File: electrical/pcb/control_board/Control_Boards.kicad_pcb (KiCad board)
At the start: 2 copper layers, 220 x 367.6 mm, 141 parts, among them J1 XT30-M, J10 Molex_172675-0613, J11 Molex_172675-0613, J13 Molex_172675-0613, J14 Molex_172675-0613, J16 277-11404-ND, J17 277-11404-ND, J18 277-11404-ND, J19 TSW-104-07-F-T, J2 ED2580-ND, J20 PEC08SAAN, J21 PPTC102LFBN-RC, J22 S9175-ND_rpi_breakout, J23 S9175-ND_rpi_breakout, J24 6posheader, J25 SSW-104-01-F-T, J26 WM6548-ND, J27 PPTC021LFBN-RC, J28 PPTC021LFBN-RC, J29 PPTC021LFBN-RC, J3 XT30-F, J30 PEC08SAAN, J4 XT30-F, J5 XT30-M, J6 ED2580-ND, J8 Molex_172675-0613, J9 Molex_172675-0613, M1 Mounting_Holes, Q1 2N3906, Q2 2N3906, Q3 2N3906, Q4 2N3906, Q5 2N3906, Q6 2N3906, SW1 CT206124-ND, T1 test_point, T10 test_point, T11 test_point, T12 test_point, T13 test_point, T14 test_point, T15 test_point, T2 test_point, T3 test_point, T4 test_point, T5 test_point, T6 test_point, T7 test_point, T8 test_point, T9 test_point, U1 INA260, U2 PCA9685, U3 D24V22Fx, U4 D24V150Fx, U5 DC7G3HWA, U6 DC7G3HWA, U7 MIC2937A-3.3WT, y1 rover_silkscreen

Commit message: updates
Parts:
- moved J17 89.4 mm to (214.3, 85.7), turned to 90 degrees
- moved RC2 63.3 mm to (145.8, 59.3), turned to 270 degrees
- moved C3 31.4 mm to (97.1, 90.6), turned to 90 degrees
- moved R21 22.9 mm to (66.0, 34.4), turned to 90 degrees
- moved C13 18.0 mm to (192.2, 70.9), turned to 180 degrees
- moved C15 18.0 mm to (192.2, 74.1), turned to 180 degrees
- moved C17 17.9 mm to (192.2, 77.2), turned to 180 degrees
- moved C20 17.9 mm to (192.2, 80.4), turned to 180 degrees
- moved C2 17.8 mm to (156.2, 70.8), turned to 0 degrees
- moved C4 11.2 mm to (156.2, 74.1), turned to 0 degrees
- moved C1 5.28 mm to (118.7, 49.0)
- moved RC1 5.16 mm to (202.6, 59.3)
- moved J16 4.97 mm to (132.1, 78.3)
- moved R5 4.78 mm to (122.0, 56.6)
- moved C9 4.68 mm to (156.2, 77.5), turned to 0 degrees
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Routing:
- net /Motor Board/E_STOP3: track 0.00 -> 417.0 mm, vias 0 -> 6
- net /Motor Board/E_STOP2: track 0.00 -> 403.5 mm, vias 0 -> 7
- net /Motor Board/E_STOP: track 0.00 -> 398.3 mm, vias 0 -> 6
- net /Motor Board/RXD: track 0.00 -> 347.5 mm, vias 0 -> 4
- net /Motor Board/TXD: track 0.00 -> 342.0 mm, vias 0 -> 4
- net /Motor Board/BATTPOS: track 0.00 -> 300.1 mm, vias 0 -> 7
- net +3.3V_motor: track 212.6 -> 402.2 mm, vias 6 -> 11
- net /Motor Board/RC2M1A: track 172.1 -> 296.4 mm, vias 4 -> 6
- net /Motor Board/alert: track 0.00 -> 118.2 mm, vias 0 -> 4
- net /Motor Board/RC2M1B: track 171.6 -> 289.5 mm, vias 4 -> 6
- net +BATT: track 0.00 -> 104.7 mm, vias 0 -> 3
- net /Motor Board/RC2M2A: track 155.9 -> 255.5 mm, vias 4 -> 6
- net /Motor Board/SDA_rpi: track 0.00 -> 97.7 mm, vias 0 -> 5
- net /Motor Board/SCL_rpi: track 0.00 -> 95.1 mm, vias 0 -> 5
- net /Motor Board/RC2M2B: track 163.6 -> 255.8 mm, vias 4 -> 6
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
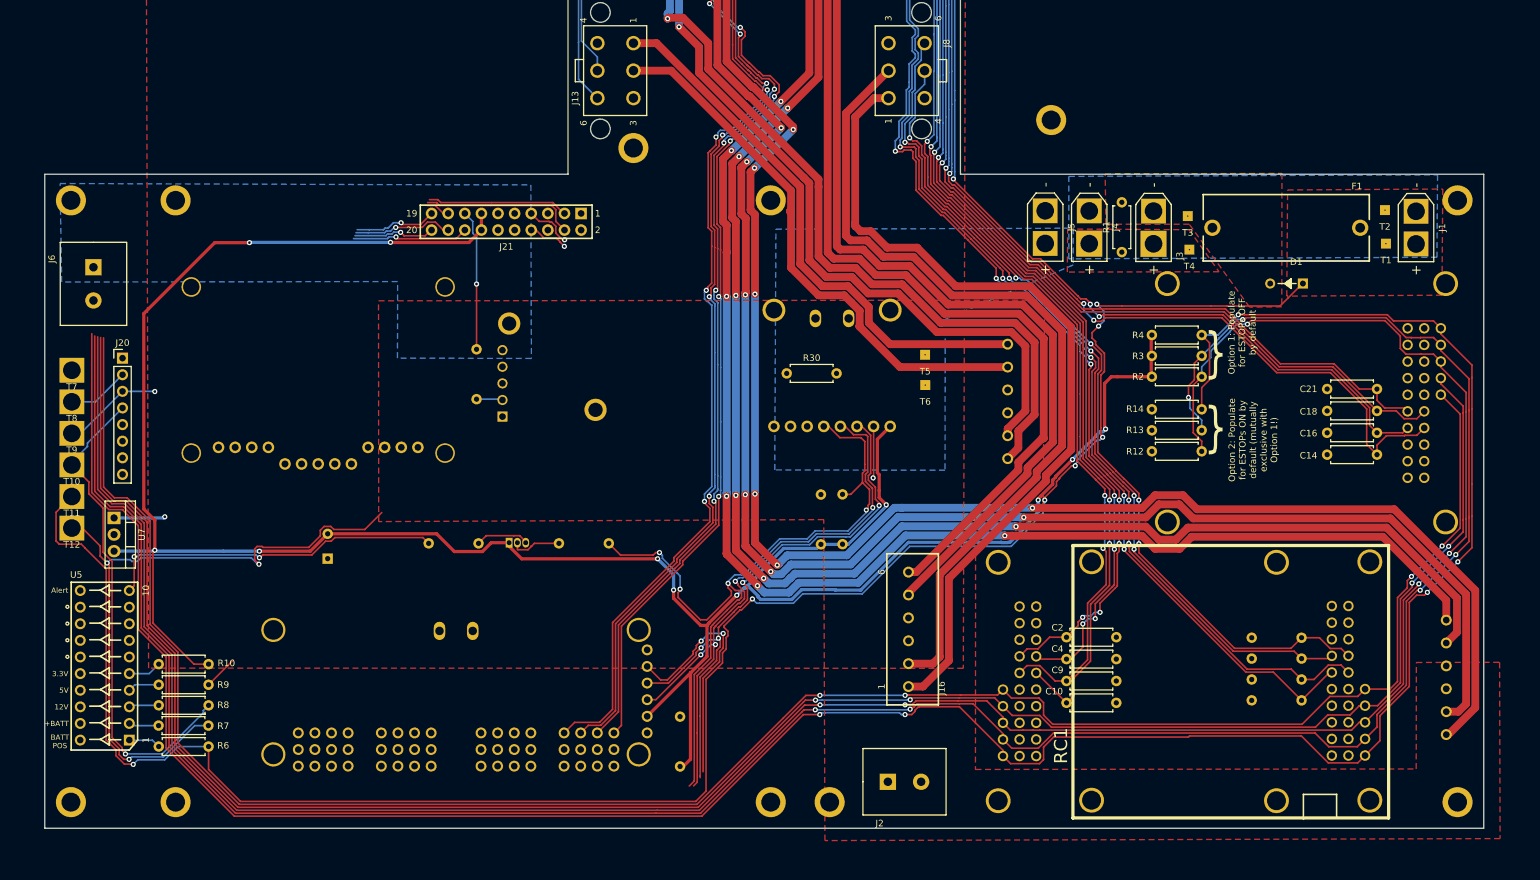
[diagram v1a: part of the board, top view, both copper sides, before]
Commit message: finished routing of motor board
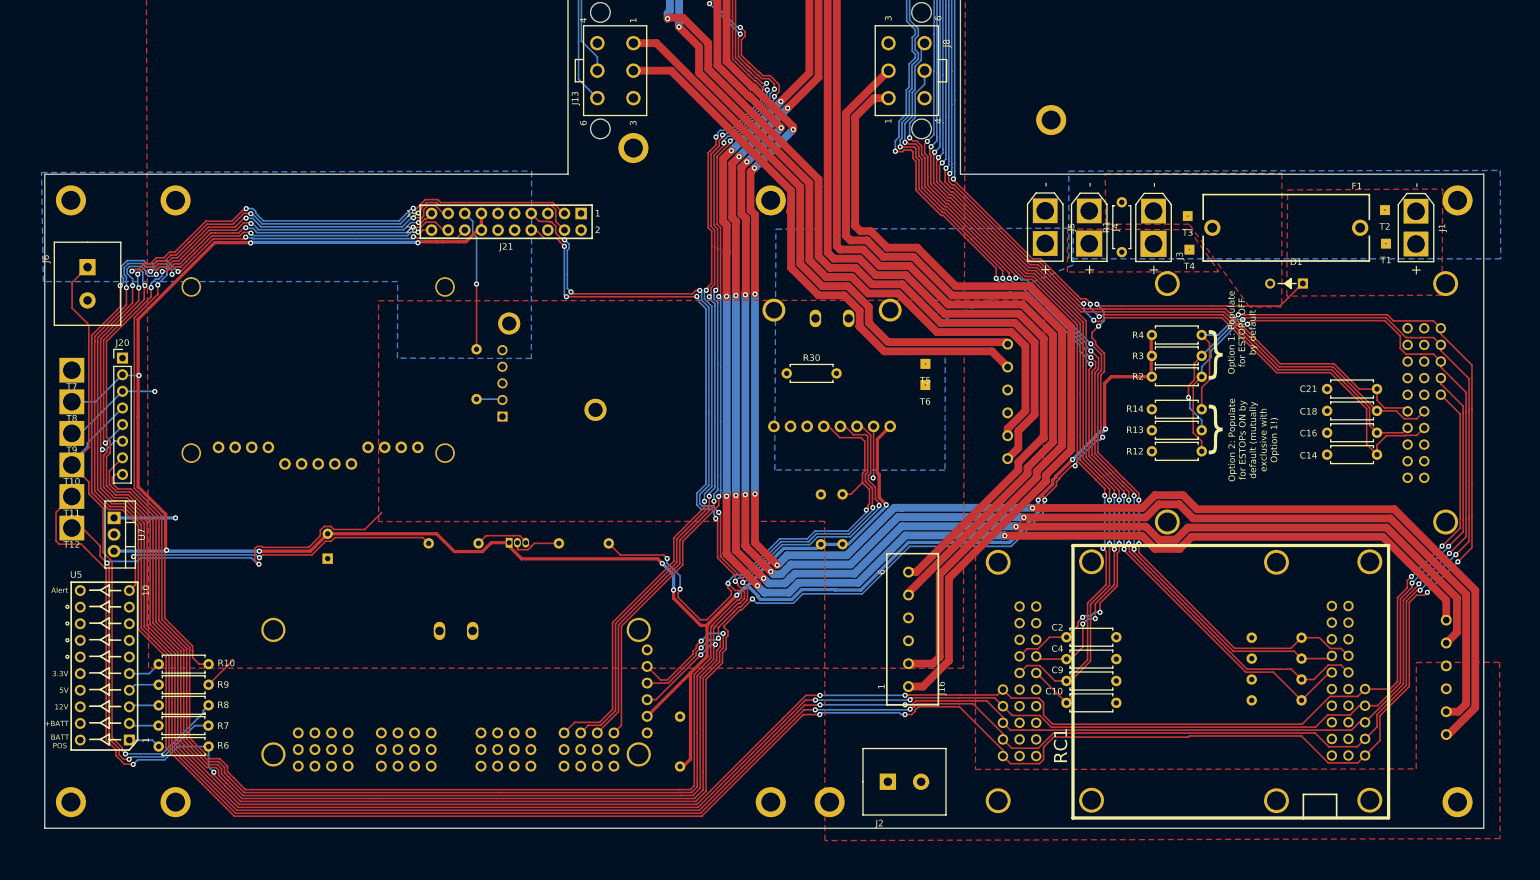
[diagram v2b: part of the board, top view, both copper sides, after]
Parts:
- moved T5 1.39 mm to (134.6, 29.0)
- moved J6 0.90 mm to (6.54, 14.2)
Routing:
- net /Motor Board/SCL_rpi: track 95.1 -> 308.1 mm, vias 5 -> 8
- net /Motor Board/alert: track 118.2 -> 327.3 mm, vias 4 -> 8
- net /Motor Board/SDA_rpi: track 97.7 -> 303.4 mm, vias 5 -> 8
- net /Motor Board/OEservos: track 53.6 -> 255.8 mm, vias 3 -> 6
- net /Motor Board/TXD: track 342.0 -> 413.3 mm, vias 4 -> 9
- net /Motor Board/RXD: track 347.5 -> 414.3 mm, vias 4 -> 9
- net /Motor Board/E_STOP: track 398.3 -> 451.4 mm, vias 6 -> 9
- net /Motor Board/E_STOP2: track 403.5 -> 456.0 mm, vias 7 -> 10
- net /Motor Board/E_STOP3: track 417.0 -> 468.5 mm, vias 6 -> 9
- net +12V_motor: track 75.5 -> 108.8 mm
- net +3.3V_motor: track 402.2 -> 404.7 mm, vias 11 -> 12
- net +5V_motor: track 36.1 -> 37.7 mm
- net /Motor Board/servo_pwm_ch3: track 187.6 -> 187.1 mm
- net /Motor Board/BATTPOS: track 300.1 -> 300.2 mm, vias 7 -> 8

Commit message: progress on brain board
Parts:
- moved R11 29.5 mm to (96.1, -190.0)
- moved J25 9.34 mm to (92.6, -171.4), turned to 90 degrees
- moved SW1 4.81 mm to (103.4, -215.5)
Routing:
- net GND_brain: track 0.00 -> 90.8 mm
- net /Brain Board/E_STOP: track 0.00 -> 61.6 mm
- net /Brain Board/E_STOP3: track 0.00 -> 59.4 mm
- net /Brain Board/E_STOP2: track 0.00 -> 54.0 mm
- net /Brain Board/SCL_rpi: track 0.00 -> 40.0 mm, vias 0 -> 1
- net /Brain Board/SDA_rpi: track 0.00 -> 36.2 mm, vias 0 -> 1
- net /Brain Board/OEservos: track 0.00 -> 34.7 mm
- net /Brain Board/12V_EN: track 0.00 -> 32.9 mm
- net /Brain Board/alert: track 0.00 -> 30.2 mm
- net +12V_brain: track 0.00 -> 28.0 mm, vias 0 -> 1
- net +5V_brain: track 0.00 -> 25.2 mm
- net /Brain Board/3.3V_rpi: track 0.00 -> 22.7 mm
- net /Brain Board/X_RPI_SPI_MISO: track 0.00 -> 11.3 mm
- net /Brain Board/X_RPI_SPI_CLK: track 0.00 -> 11.3 mm
- net /Brain Board/X_RPI_GPIO_GCLK: track 0.00 -> 11.3 mm
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- added copper zone on F.Cu, net +3.3V_brain
- added copper zone on B.Cu, net GND_brain

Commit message: progress on brain board
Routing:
- net +5V_brain: track 25.2 -> 155.4 mm, vias 0 -> 5
- net /Brain Board/RXD: track 11.3 -> 135.9 mm, vias 0 -> 5
- net /Brain Board/TXD: track 11.3 -> 133.1 mm, vias 0 -> 5
- net /Brain Board/SDA_rpi: track 36.2 -> 147.0 mm, vias 1 -> 3
- net /Brain Board/SCL_rpi: track 40.0 -> 145.8 mm, vias 1 -> 5
- net /Brain Board/OEservos: track 34.7 -> 134.7 mm, vias 0 -> 1
- net +12V_brain: track 28.0 -> 126.7 mm, vias 1 -> 3
- net /Brain Board/alert: track 30.2 -> 91.4 mm
- net /Brain Board/12V_EN: track 32.9 -> 92.5 mm
- net /Brain Board/ESTOP_in_2: track 0.00 -> 41.3 mm
- net /Brain Board/E_STOP3: track 59.4 -> 97.6 mm
- net /Brain Board/ESTOP_in_3: track 0.00 -> 38.2 mm, vias 0 -> 1
- net /Brain Board/E_STOP2: track 54.0 -> 88.0 mm
- net /Brain Board/E_STOP: track 61.6 -> 91.3 mm

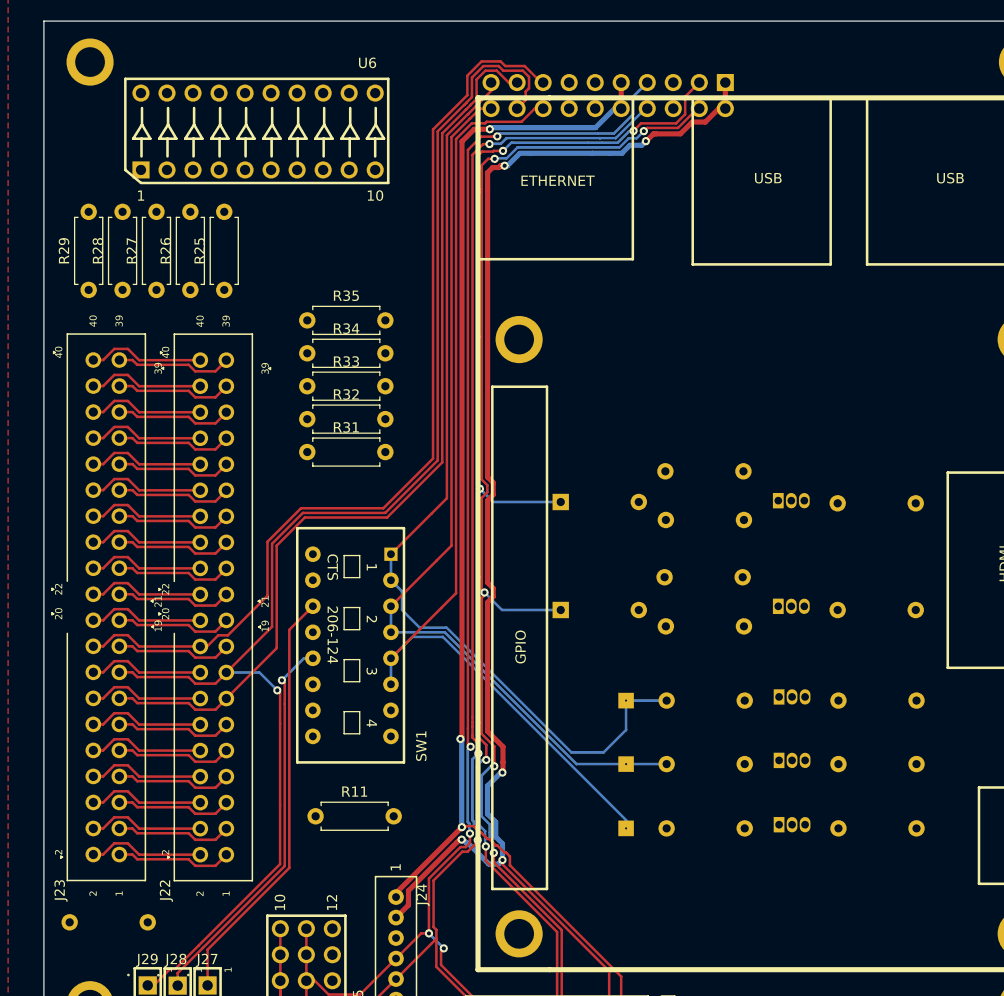
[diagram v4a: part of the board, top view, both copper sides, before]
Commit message: Finished routing brain board
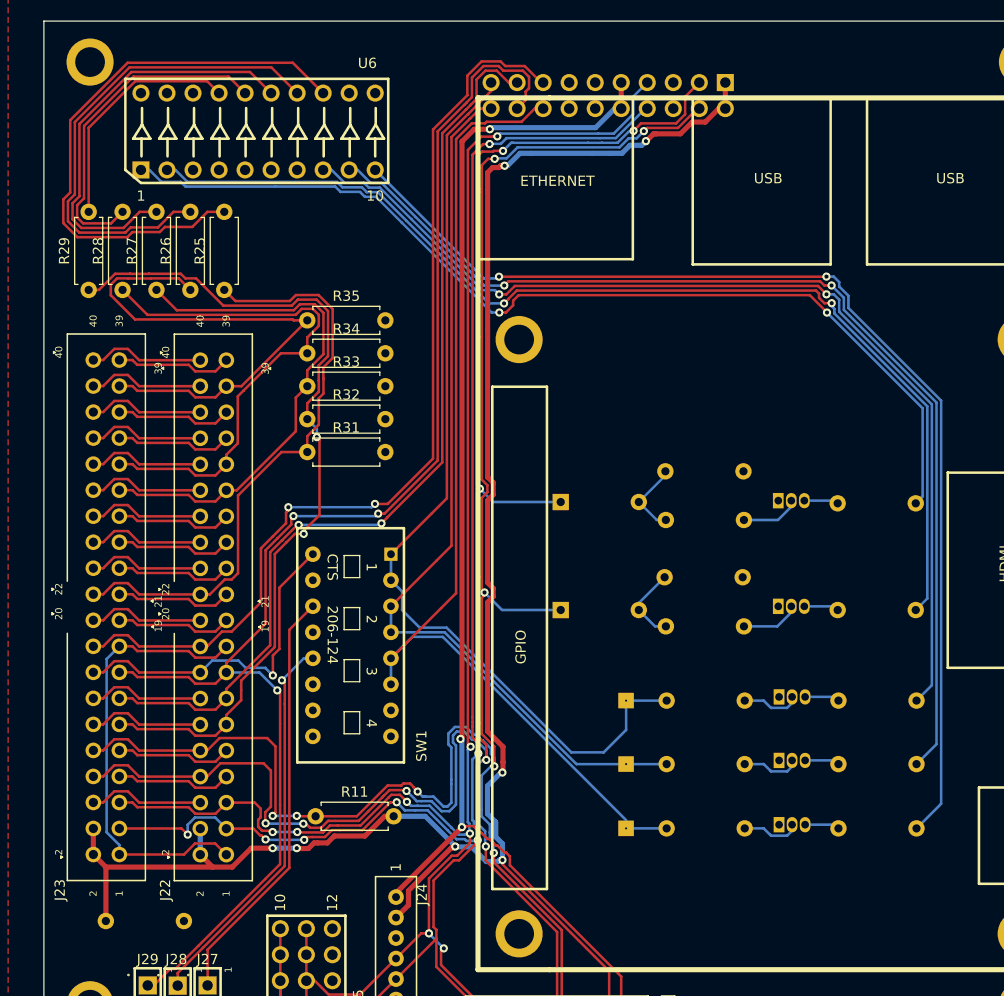
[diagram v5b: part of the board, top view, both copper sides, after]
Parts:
- moved C32 3.53 mm to (75.6, -179.7)
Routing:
- net /Brain Board/ESTOP_LED_3: track 0.00 -> 108.4 mm, vias 0 -> 2
- net /Brain Board/RXD_LED: track 0.00 -> 106.1 mm, vias 0 -> 2
- net /Brain Board/ESTOP_LED_2: track 0.00 -> 103.9 mm, vias 0 -> 2
- net /Brain Board/ESTOP_LED_1: track 0.00 -> 99.8 mm, vias 0 -> 2
- net /Brain Board/TXD_LED: track 0.00 -> 97.2 mm, vias 0 -> 2
- net /Brain Board/RPI_LED_5: track 11.3 -> 83.3 mm, vias 0 -> 2
- net Net-(R25-Pad2): track 0.00 -> 55.9 mm
- net /Brain Board/RXD: track 135.9 -> 184.9 mm, vias 5 -> 8
- net Net-(R26-Pad2): track 0.00 -> 48.1 mm
- net /Brain Board/RPI_LED_1: track 11.3 -> 58.8 mm
- net /Brain Board/TXD: track 133.1 -> 179.6 mm, vias 5 -> 8
- net /Brain Board/RPI_LED_4: track 11.3 -> 51.8 mm
- net Net-(R27-Pad2): track 0.00 -> 40.4 mm
- net /Brain Board/RPI_LED_2: track 11.3 -> 51.6 mm
- net /Brain Board/RPI_LED_3: track 11.3 -> 50.9 mm
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
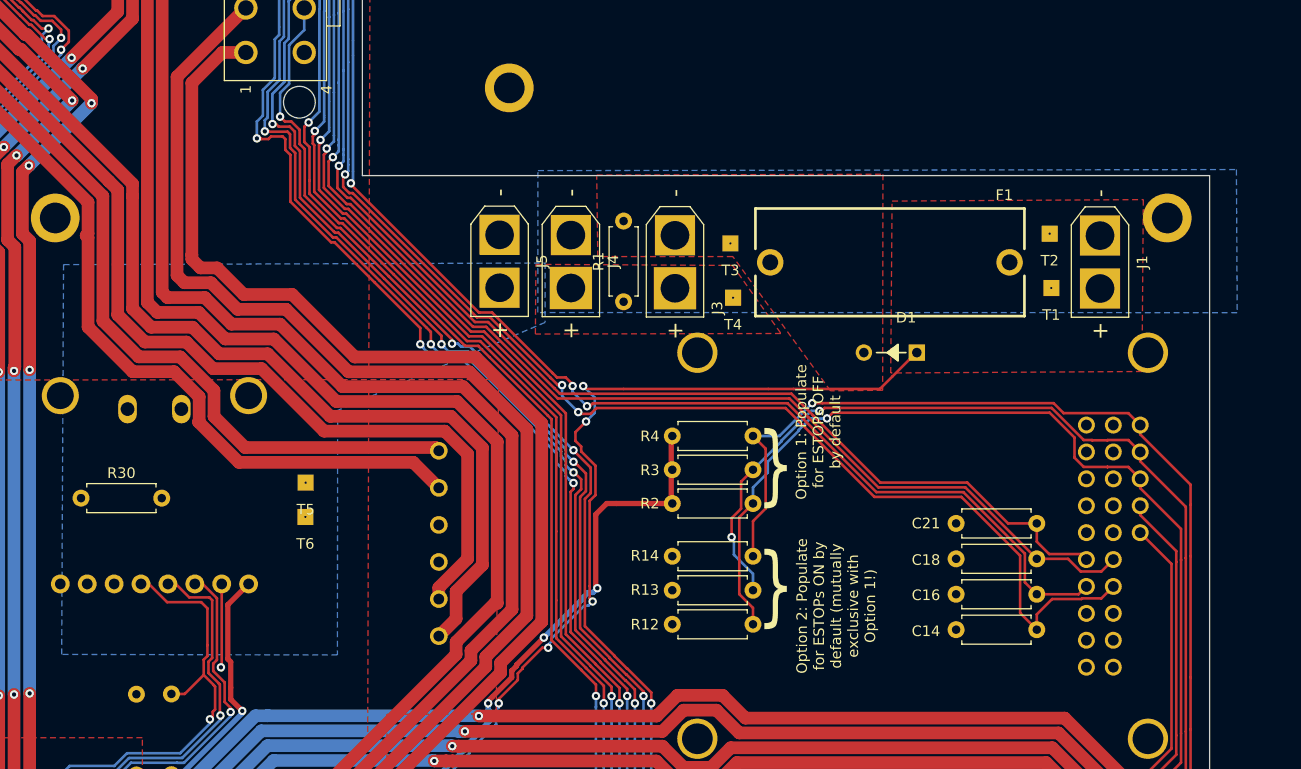
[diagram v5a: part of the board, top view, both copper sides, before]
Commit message: updating spacing of power connectors for ease of access
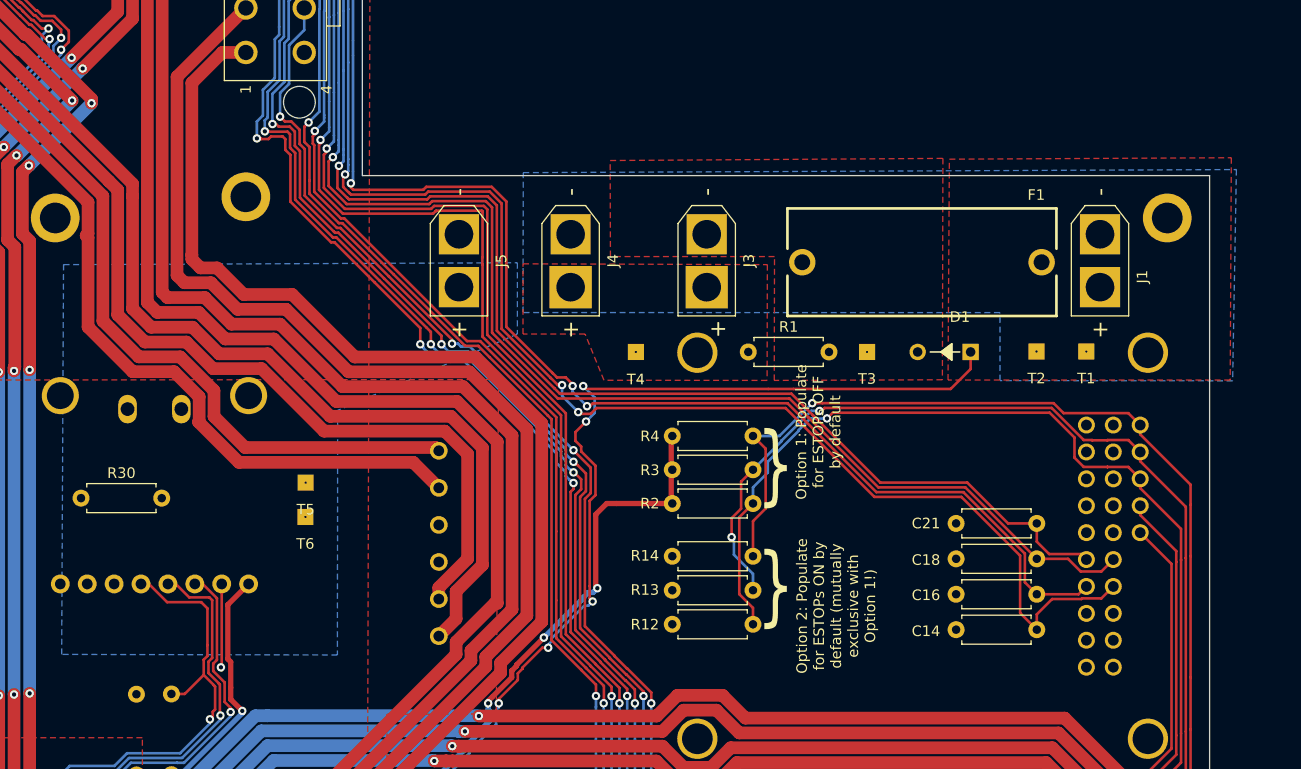
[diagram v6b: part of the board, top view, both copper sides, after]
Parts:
- moved MH17 26.9 mm to (129.0, 2.00)
- moved T3 16.5 mm to (187.7, 16.7)
- moved R1 12.7 mm to (176.4, 16.7), turned to 0 degrees
- moved T2 11.2 mm to (203.7, 16.6)
- moved T4 10.5 mm to (165.8, 16.7)
- moved T1 6.84 mm to (208.4, 16.6)
- moved D1 5.08 mm to (197.4, 16.7)
- moved J5 3.84 mm to (149.1, 5.54)
- moved F1 3.02 mm to (192.8, 8.18)
- moved J3 3.00 mm to (172.5, 5.54)
- moved J1 0.13 mm to (209.7, 5.54)
- moved J4 0.08 mm to (159.7, 5.54)
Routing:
- net /Motor Board/RC3EN1B: track 281.1 -> 288.5 mm
- net /Motor Board/RC2EN1B: track 232.5 -> 239.7 mm
- net /Motor Board/RC2EN1A: track 231.2 -> 238.4 mm
- net /Motor Board/RC3EN2A: track 252.3 -> 259.4 mm
- net /Motor Board/RC3EN2B: track 253.4 -> 260.5 mm
- net /Motor Board/RC3EN1A: track 284.3 -> 291.5 mm
- net /Motor Board/BATTPOS: track 300.2 -> 305.8 mm
